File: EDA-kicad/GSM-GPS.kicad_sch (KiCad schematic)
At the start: 3 parts, among them J2 SIM-G85D1160022HHR, U1 GSM-GPS-EC25VFA-512-STD, U2 EG25GGC-128-SGNS

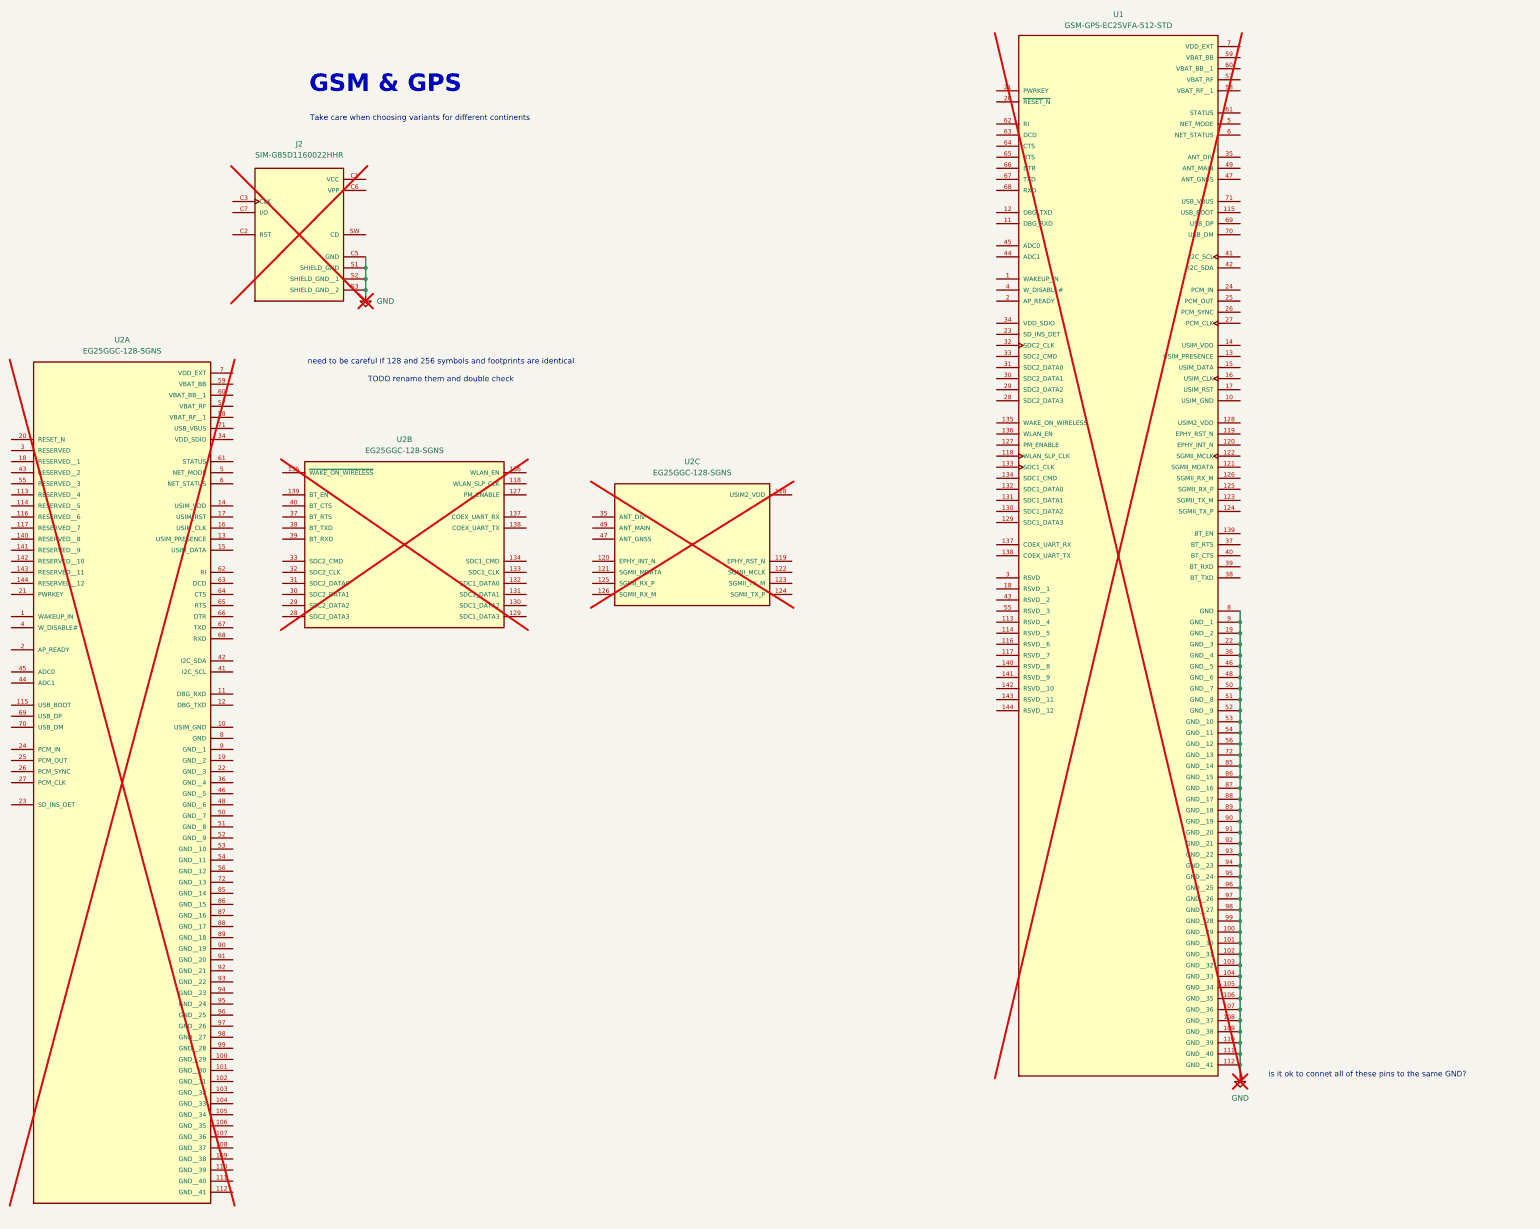
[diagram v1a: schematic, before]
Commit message: Improve KiCAD schematic design and labeling
- Replace overused global labels with hierarchical and local labels
- Add proper GND connections to components
- Fix BACKLIGHT- net issues
- Apply minor schematic fixes and cleanups
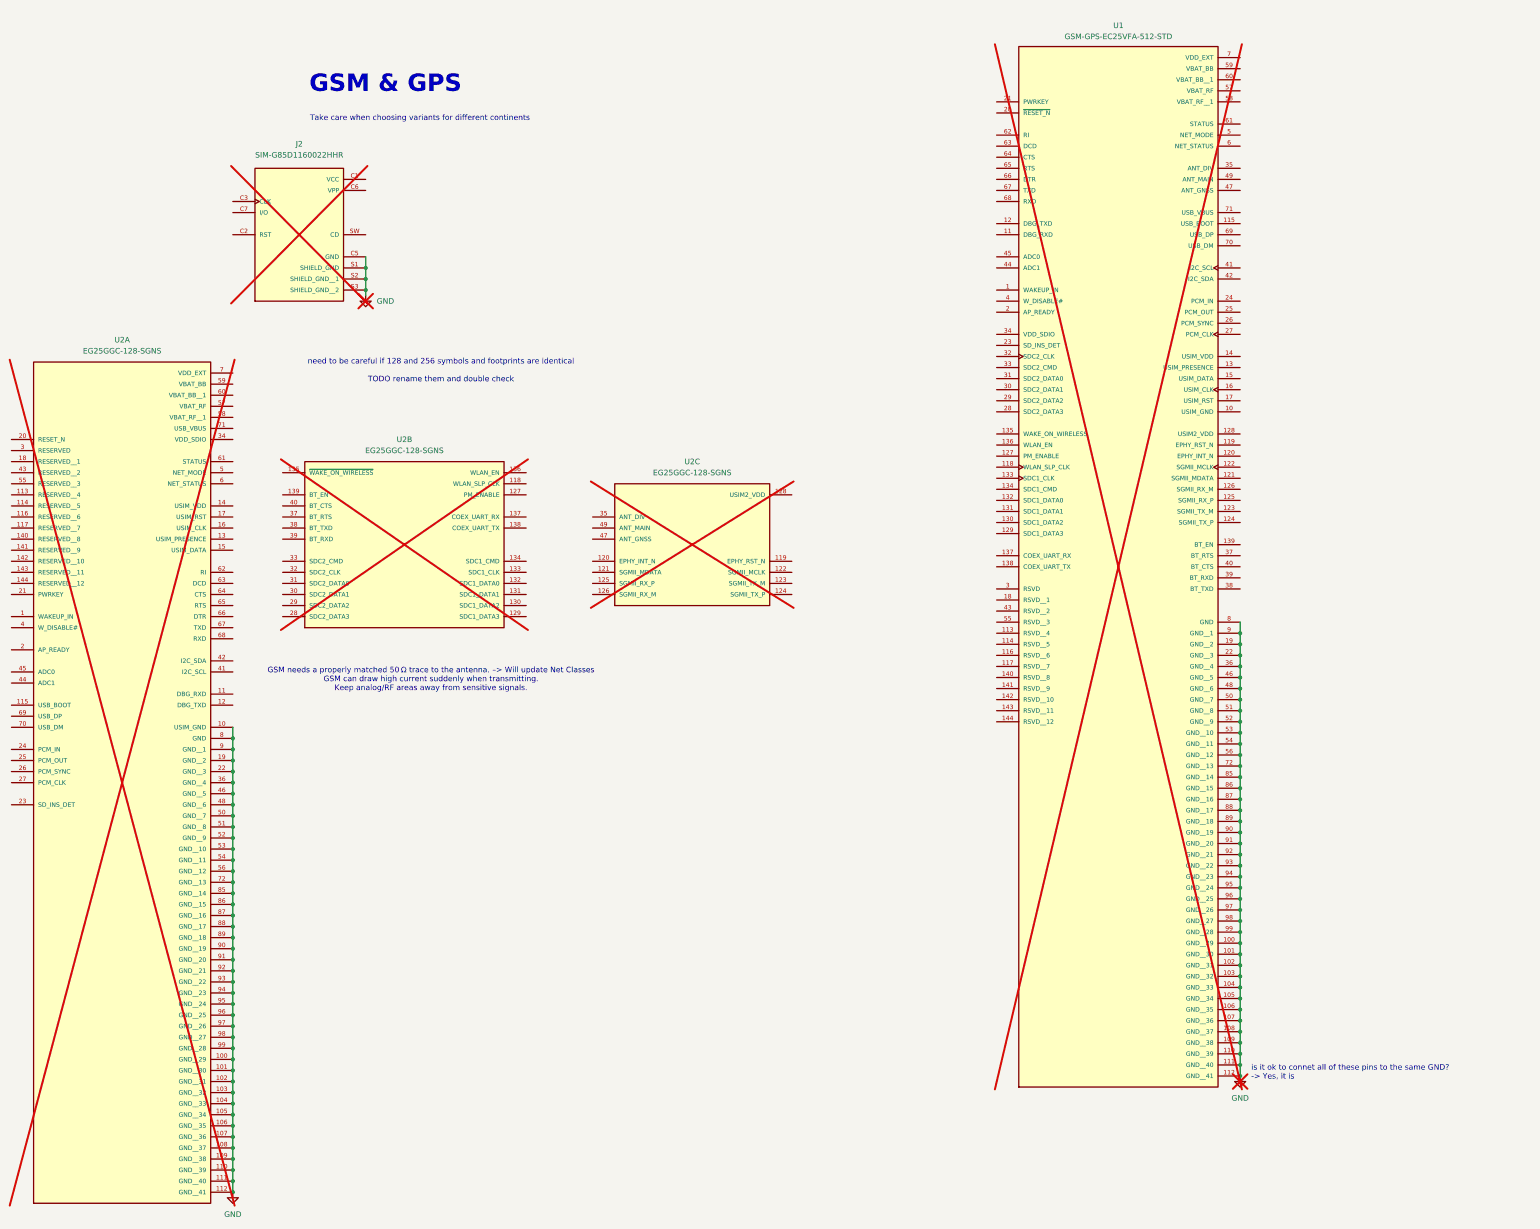
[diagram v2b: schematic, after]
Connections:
- net GND: now also U2.10 (USIM_GND), U2.100 (GND__29), U2.101 (GND__30), U2.102 (GND__31), U2.103 (GND__32), U2.104 (GND__33), U2.105 (GND__34), U2.106 (GND__35), U2.107 (GND__36), U2.108 (GND__37), U2.109 (GND__38), U2.110 (GND__39), U2.111 (GND__40), U2.112 (GND__41), U2.19 (GND__2), U2.22 (GND__3), U2.36 (GND__4), U2.46 (GND__5), U2.48 (GND__6), U2.50 (GND__7), U2.51 (GND__8), U2.52 (GND__9), U2.53 (GND__10), U2.54 (GND__11), U2.56 (GND__12), U2.72 (GND__13), U2.8 (GND), U2.85 (GND__14), U2.86 (GND__15), U2.87 (GND__16), U2.88 (GND__17), U2.89 (GND__18), U2.9 (GND__1), U2.90 (GND__19), U2.91 (GND__20), U2.92 (GND__21), U2.93 (GND__22), U2.94 (GND__23), U2.95 (GND__24), U2.96 (GND__25), U2.97 (GND__26), U2.98 (GND__27), U2.99 (GND__28)
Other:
- note added: "GSM needs a properly matched 50 Ω trace to the antenna. –> Will update Net Classes GSM can draw high current suddenly when transmitting. Keep analog/RF areas away from sensitive signals."
- note added: "is it ok to connet all of these pins to the same GND? -> Yes, it is"
- note removed: "is it ok to connet all of these pins to the same GND?"
- moved on the sheet: U1
